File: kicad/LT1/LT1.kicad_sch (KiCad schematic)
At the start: 12 parts, among them J1 USB_B, U1 MCP73831-2-OT, U2 TLV75533PDBV, U3 STM32L412CBTxP, Y1 Crystal

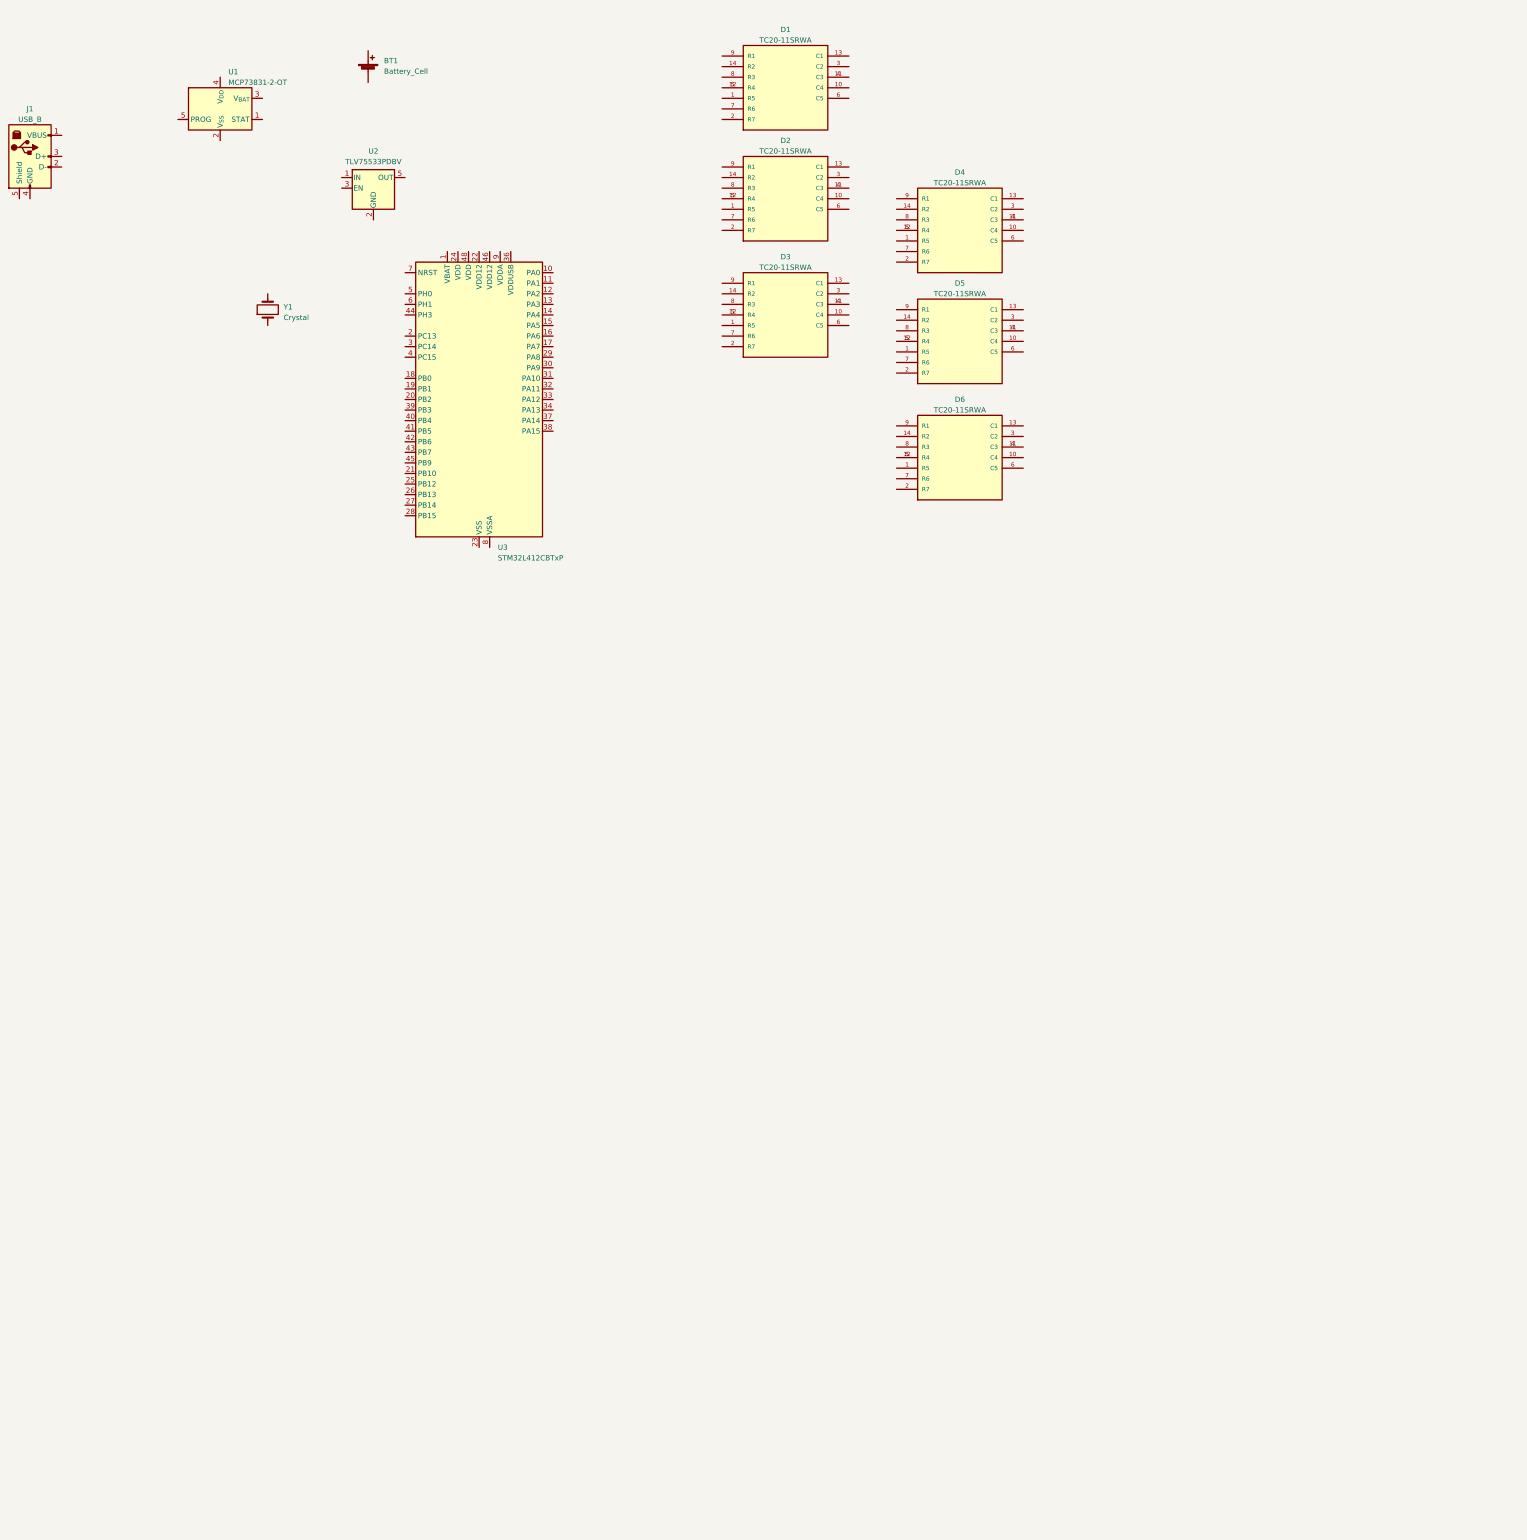
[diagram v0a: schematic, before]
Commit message: schematics: added led matrix display, did much on MCU
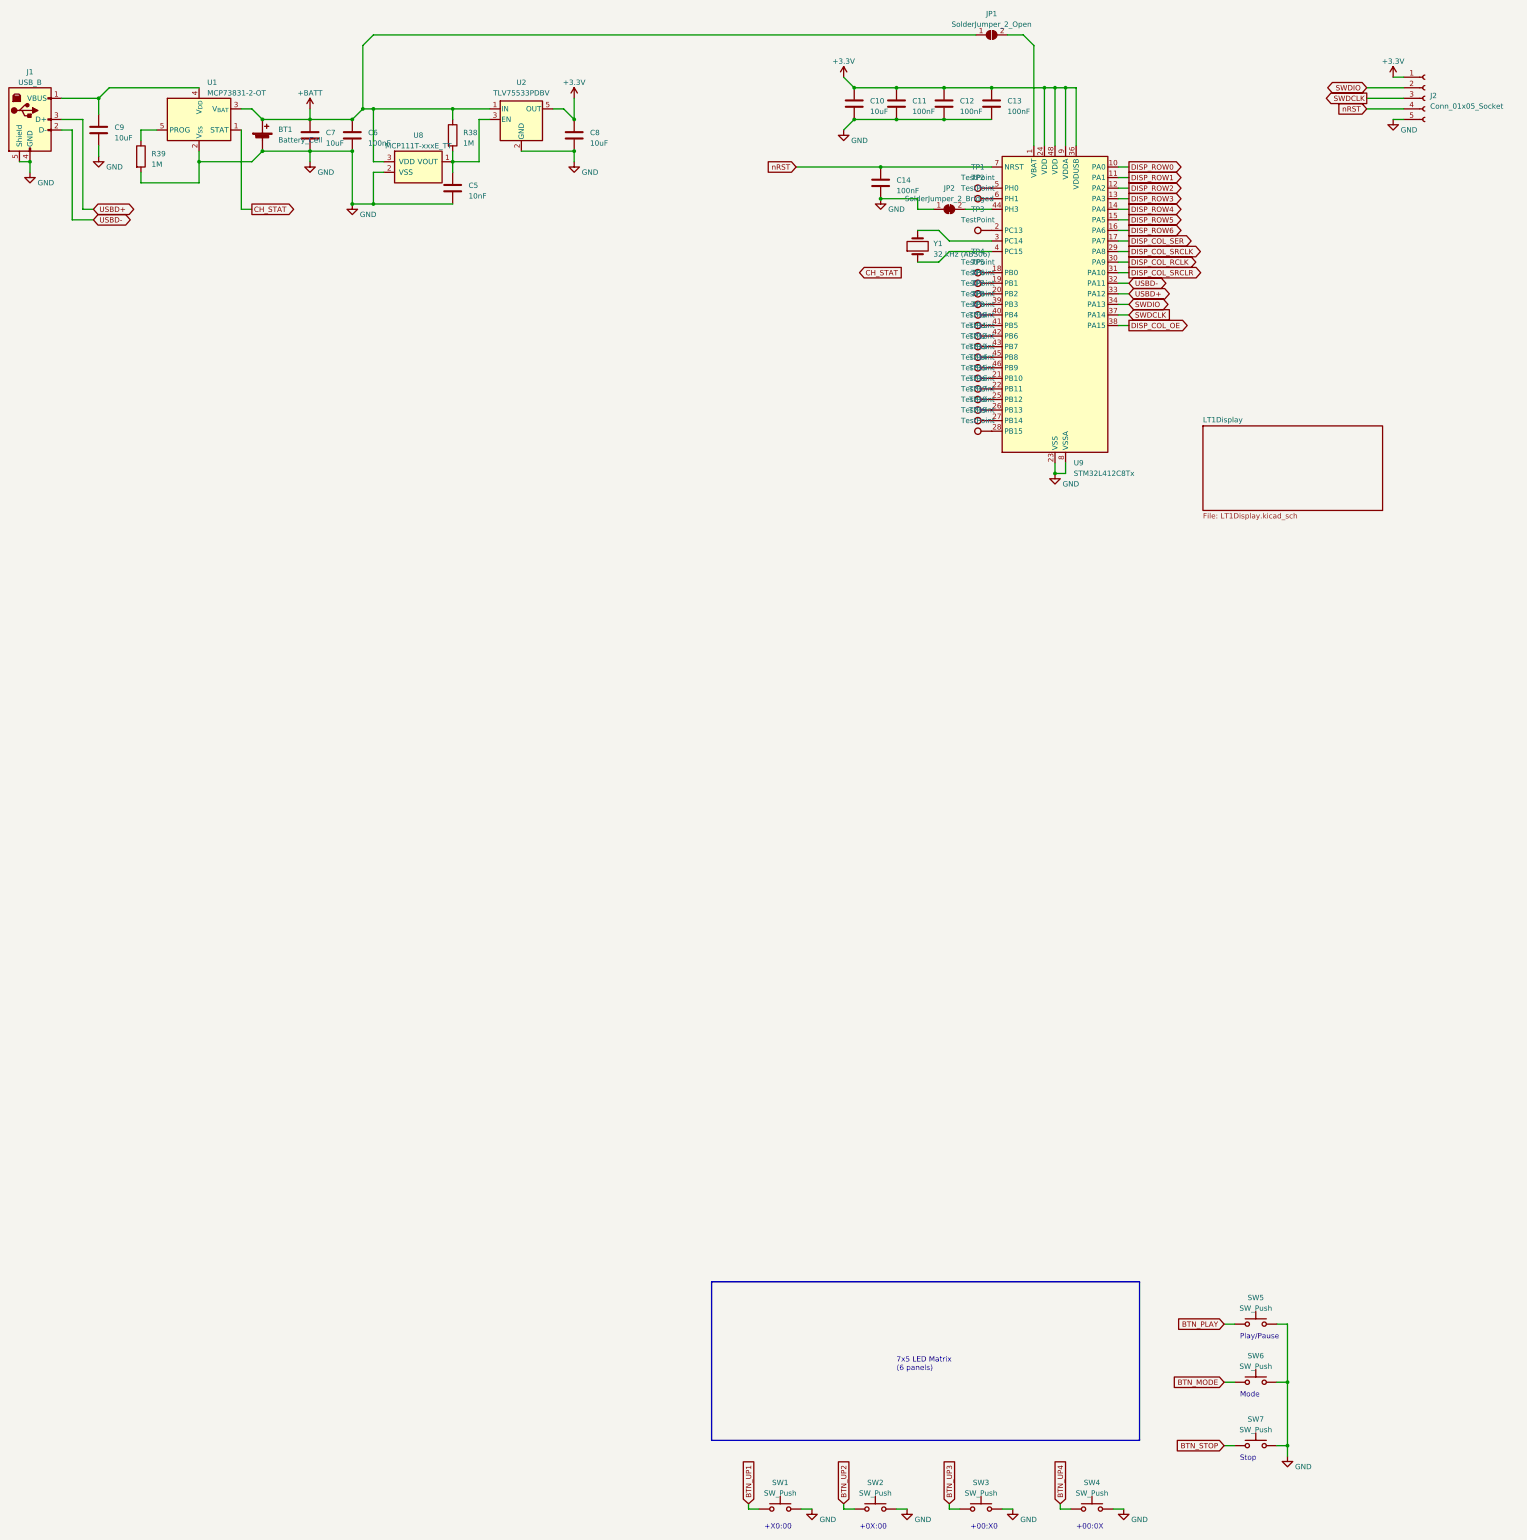
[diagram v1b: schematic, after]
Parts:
- removed D1, D2, D3, D4, D5, D6: TC20-11SRWA, TC20-11SRWA:LED_TC20-11SRWA, symbol TC20-11SRWA:TC20-11SRWA
- removed U3: STM32L412CBTxP, Package_QFP:LQFP-48_7x7mm_P0.5mm, symbol MCU_ST_STM32L4:STM32L412CBTxP
- added C10, C7, C8, C9: 10uF, symbol Device:C
- added C11, C12, C13, C14, C6: 100nF, symbol Device:C
- added C5: 10nF, symbol Device:C
- added J2: Conn_01x05_Socket, symbol Connector:Conn_01x05_Socket
- added JP1: SolderJumper_2_Open, symbol Jumper:SolderJumper_2_Open
- added JP2: SolderJumper_2_Bridged, symbol Jumper:SolderJumper_2_Bridged
- added R38, R39: 1M, symbol Device:R
- added SW1, SW2, SW3, SW4, SW5, SW6, SW7: SW_Push, symbol Switch:SW_Push
- added TP1, TP10, TP11, TP12, TP13, TP14, TP15, TP16, TP17, TP18, TP19, TP2, TP3, TP4, TP5, TP6, TP7, TP8, TP9: TestPoint, symbol Connector:TestPoint
- added U8: MCP111T-xxxE_TT, symbol MEgliParts:MCP111T-xxxE_TT
- added U9: STM32L412C8Tx, Package_QFP:LQFP-48_7x7mm_P0.5mm, symbol MCU_ST_STM32L4:STM32L412C8Tx
- Y1: value Crystal -> 32 kHz (ABS06)
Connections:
- net at Y1.1: now also U9.4 (PC15)
- net at Y1.2: now also U9.3 (PC14)
- net at J1.1 (VBUS): now also U1.4 (V_{DD}), C9.1
- net USBD-: now reaches J1.2 (D-)
- net USBD-: now also U9.32 (PA11)
- net USBD+: now reaches J1.3 (D+)
- net USBD+: now also U9.33 (PA12)
- net GND: now reaches J1.4 (GND)
- net GND: now also BT1.2 (-), J1.5 (Shield), U1.2 (V_{SS}), U2.2 (GND), C10.2, C11.2, C12.2, C13.2, C14.2, C5.2, C6.2, C7.2, C8.2, C9.2, J2.5 (Pin_5), JP2.1 (A), R39.2, SW1.2, SW2.2, SW3.2, SW4.2, SW5.2, SW6.2, SW7.2, U8.2 (VSS), U9.23 (VSS), U9.35 (VSS), U9.47 (VSS), U9.8 (VSSA)
- net CH_STAT: now reaches U1.1 (STAT)
- net +BATT: now reaches U1.3 (V_{BAT})
- net +BATT: now also BT1.1 (+), U2.1 (IN), C6.1, C7.1, JP1.1 (A), R38.1, U8.3 (VDD)
- net at U1.5 (PROG): now also R39.1
- net at U2.3 (EN): now also C5.1, R38.2, U8.1 (VOUT)
- net +3.3V: now reaches U2.5 (OUT)
- net +3.3V: now also C10.1, C11.1, C12.1, C13.1, C8.1, J2.1 (Pin_1), U9.24 (VDD), U9.36 (VDDUSB), U9.48 (VDD), U9.9 (VDDA)
- new net: TP1.1, U9.5 (PH0)
- new net: TP11.1, U9.43 (PB7)
- new net: TP5.1, U9.19 (PB1)
- new net: TP18.1, U9.27 (PB14)
- new net: JP1.2 (B), U9.1 (VBAT)
- new net: TP4.1, U9.18 (PB0)
- new net: TP3.1, U9.2 (PC13)
- new net: TP6.1, U9.20 (PB2)
- new net: TP14.1, U9.21 (PB10)
- new net: TP15.1, U9.22 (PB11)
- new net: TP16.1, U9.25 (PB12)
- new net: TP17.1, U9.26 (PB13)
- new net: TP19.1, U9.28 (PB15)
- new net: TP7.1, U9.39 (PB3)
- new net: TP8.1, U9.40 (PB4)
- new net: TP9.1, U9.41 (PB5)
- new net: TP10.1, U9.42 (PB6)
- new net: JP2.2 (B), U9.44 (PH3)
- new net: TP12.1, U9.45 (PB8)
- new net: TP13.1, U9.46 (PB9)
- new net: TP2.1, U9.6 (PH1)
- new net BTN_MODE: SW6.1
- new net BTN_PLAY: SW5.1
- new net BTN_STOP: SW7.1
- new net BTN_UP1: SW1.1
- new net BTN_UP2: SW2.1
- new net BTN_UP3: SW3.1
- new net BTN_UP4: SW4.1
- new net DISP_COL_OE: U9.38 (PA15)
- new net DISP_COL_RCLK: U9.30 (PA9)
- new net DISP_COL_SER: U9.17 (PA7)
- new net DISP_COL_SRCLK: U9.29 (PA8)
- new net DISP_COL_SRCLR: U9.31 (PA10)
- new net DISP_ROW0: U9.10 (PA0)
- new net DISP_ROW1: U9.11 (PA1)
- new net DISP_ROW2: U9.12 (PA2)
- new net DISP_ROW3: U9.13 (PA3)
- new net DISP_ROW4: U9.14 (PA4)
- new net DISP_ROW5: U9.15 (PA5)
- new net DISP_ROW6: U9.16 (PA6)
- new net SWDCLK: J2.3 (Pin_3), U9.37 (PA14)
- new net SWDIO: J2.2 (Pin_2), U9.34 (PA13)
- new net nRST: C14.1, J2.4 (Pin_4), U9.7 (NRST)
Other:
- added sheet LT1Display (LT1Display.kicad_sch)
- note added: "+00:0X"
- note added: "+00:X0"
- note added: "+0X:00"
- note added: "+X0:00"
- note added: "7x5 LED Matrix (6 panels)"
- note added: "Mode"
- note added: "Play/Pause"
- note added: "Stop"
- moved on the sheet: BT1, J1, U1, U2, Y1

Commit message: LT1 schema done
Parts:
- added R40, R41: 10k, symbol Device:R
- added S1: ~, symbol switch1:5Pol_switch
- added TP20, TP21, TP22, TP23, TP24, TP25, TP26, TP27, TP28, TP29, TP30, TP31: TestPoint, symbol Connector:TestPoint
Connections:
- net BTN_MODE: now also TP9.1, U9.41 (PB5)
- net BTN_PLAY: now also TP8.1, U9.40 (PB4)
- net BTN_STOP: now also TP10.1, U9.42 (PB6)
- net BTN_UP1: now also TP4.1, U9.18 (PB0)
- net BTN_UP2: now also TP5.1, U9.19 (PB1)
- net BTN_UP3: now also TP6.1, U9.20 (PB2)
- net BTN_UP4: now also TP7.1, U9.39 (PB3)
- net CH_STAT: now also TP11.1, U9.43 (PB7)
- net DISP_COL_OE: now also TP31.1
- net DISP_COL_RCLK: now also TP29.1
- net DISP_COL_SER: now also TP27.1
- net DISP_COL_SRCLK: now also TP28.1
- net DISP_COL_SRCLR: now also TP30.1
- net DISP_ROW0: now also TP20.1
- net DISP_ROW1: now also TP21.1
- net DISP_ROW2: now also TP22.1
- net DISP_ROW3: now also TP23.1
- net DISP_ROW4: now also TP24.1
- net DISP_ROW5: now also TP25.1
- net DISP_ROW6: now also TP26.1
- net GND: now also R41.2
- net SW1: now reaches TP14.1, U9.21 (PB10)
- net SW1: now also S1.2
- net SW2: now reaches TP15.1, U9.22 (PB11)
- net SW2: now also S1.3
- net SW3: now reaches TP16.1, U9.25 (PB12)
- net SW3: now also S1.4
- net SW4: now reaches TP17.1, U9.26 (PB13)
- net SW4: now also S1.5
- net USB_STAT: now reaches TP12.1, U9.45 (PB8)
- net USB_STAT: now also R40.2, R41.1
- net SW0: now reaches TP13.1, U9.46 (PB9)
- net SW0: now also S1.1
- net VBUS: now reaches C9.1, J1.1 (VBUS), U1.4 (V_{DD})
- net VBUS: now also R40.1
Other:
- moved on the sheet: BT1, C5, C6, C7, C8, C9, J1, R38, R39, SW1, SW2, SW3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

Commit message: LT1 started with PCB, added driver for piezo and vibra alarm
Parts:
- removed J1: USB_B, symbol Connector:USB_B
- added C15, C16: ~, Capacitor_SMD:C_0603_1608Metric, symbol Device:C
- added D7, D8: D_Schottky, Diode_SMD:D_SOD-123, symbol Device:D_Schottky
- added J1: USB_B_Micro, Connector_USB:USB_Micro-B_Amphenol_10104110_Horizontal, symbol Connector:USB_B_Micro
- added J3, J4: Conn_01x02_Socket, Connector_PinSocket_2.54mm:PinSocket_1x02_P2.54mm_Vertical, symbol Connector:Conn_01x02_Socket
- added Q31, Q32: 2N7002K, Package_TO_SOT_SMD:TSOT-23, symbol Transistor_FET:2N7002K
- added R42, R43: 10R, Resistor_SMD:R_0603_1608Metric, symbol Device:R
- added R44: 1k5, Resistor_SMD:R_0603_1608Metric, symbol Device:R
- added R45: 10k, Resistor_SMD:R_0603_1608Metric, symbol Device:R
- added R46, R47, R48, R49: 1M, Resistor_SMD:R_0603_1608Metric, symbol Device:R
- BT1: footprint (none) -> Connector_PinSocket_2.54mm:PinSocket_1x02_P2.54mm_Vertical
- C10, C7, C8, C9: footprint (none) -> Capacitor_SMD:C_0805_2012Metric
- C11, C12, C13, C14, C5, C6: footprint (none) -> Capacitor_SMD:C_0603_1608Metric
- J2: footprint (none) -> Connector_PinSocket_1.27mm:PinSocket_1x05_P1.27mm_Vertical
- JP1: footprint (none) -> Jumper:SolderJumper-2_P1.3mm_Open_RoundedPad1.0x1.5mm
- JP2: footprint (none) -> Jumper:SolderJumper-2_P1.3mm_Bridged_RoundedPad1.0x1.5mm
- R38, R39, R40, R41: footprint (none) -> Resistor_SMD:R_0603_1608Metric
- S1: value ~ -> MF140; footprint (none) -> Connector_PinSocket_2.54mm:PinSocket_1x05_P2.54mm_Vertical
- SW1, SW2, SW3, SW4, SW5, SW6, SW7: footprint (none) -> Button_Switch_THT:SW_PUSH_6mm_H9.5mm
- TP1, TP10, TP11, TP12, TP13, TP14, TP15, TP16, TP17, TP18, TP19, TP2, TP20, TP21, TP22, TP23, TP24, TP25, TP26, TP27, TP28, TP29, TP3, TP30, TP31, TP4, TP5, TP6, TP7, TP8, TP9: footprint (none) -> TestPoint:TestPoint_Pad_D1.0mm
- U8: footprint (none) -> Package_TO_SOT_SMD:TSOT-23
- Y1: footprint (none) -> Resistor_SMD:R_0805_2012Metric_Pad1.20x1.40mm_HandSolder
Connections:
- net +3.3V: now also D7.1 (K), D8.1 (K), J3.2 (Pin_2), J4.2 (Pin_2), R44.2
- net GND: now also C15.1, C16.1, J1.5 (GND), J1.6 (Shield), Q31.2 (S), Q32.2 (S), R45.2, R46.2, R47.2
- net USBD+: now also J1.3 (D+), R43.2; no longer U9.33 (PA12)
- net USBD-: now also J1.2 (D-), R42.2; no longer U9.32 (PA11)
- net VBUS: now also J1.1 (VBUS)
- net ALM0: now reaches TP18.1, U9.27 (PB14)
- net ALM0: now also Q31.1 (G), R46.1
- net at U9.4 (PC15), Y1.1: now also C16.2
- net at U9.3 (PC14), Y1.2: now also C15.2
- net ALM1: now reaches TP19.1, U9.28 (PB15)
- net ALM1: now also Q32.1 (G), R47.1
- new net: J3.1 (Pin_1), R48.1
- new net: D7.2 (A), Q31.3 (D), R48.2
- new net: R43.1, R44.1, U9.33 (PA12)
- new net: J1.4 (ID), R45.1
- new net: R42.1, U9.32 (PA11)
- new net: D8.2 (A), Q32.3 (D), R49.2
- new net: J4.1 (Pin_1), R49.1
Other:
- note added: "Piezo Vibra"
- moved on the sheet: J2, TP10, TP11, TP12, TP13, TP14, TP15, TP16, TP17, TP18, TP19, TP20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
